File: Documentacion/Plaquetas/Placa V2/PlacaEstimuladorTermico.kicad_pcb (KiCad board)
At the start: 2 copper layers, 119.6 x 119.6 mm, 63 parts, among them J2 BorneraGrupoTermistores, J3 BorneraTermistor, J4 BORNERA_VCC, K1 FINDER-34.51, Q1 IRF4905, Q2 IRFZ44N, Q3 IRF4905, Q4 IRFZ44N, Q5 BC337, Q6 BC337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

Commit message: I designed the pcb, it was my first try so please check every wire
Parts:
- removed D5: DIODE, Diode_THT:D_5W_P10.16mm_Horizontal
- removed D6: D_Zener, Diode_THT:D_DO-201AE_P12.70mm_Horizontal
- removed K1: FINDER-34.51, Relay_THT:Relay_SPDT_Finder_34.51_Vertical
- removed R16, R17: R, Resistor_THT:R_Axial_DIN0309_L9.0mm_D3.2mm_P15.24mm_Horizontal
- removed RV1: R_POT, Potentiometer_THT:Potentiometer_ACP_CA14-H2,5_Horizontal
- removed SW1: SW_DIP_x01, TerminalBlock:TerminalBlock_bornier-2_P5.08mm
- added C11: 4.7n, Capacitor_THT:C_Disc_D7.0mm_W2.5mm_P5.00mm, B.Cu at (88.9, 86.9)
- A1, Q6, R11, U1, U4, U5: moved to B.Cu
- C1, C2: footprint Capacitor_THT:CP_Radial_D12.5mm_P5.00mm -> Capacitor_THT:CP_Radial_D13.0mm_P7.50mm
- C10, C6: footprint Capacitor_THT:C_Disc_D9.0mm_W5.0mm_P10.00mm -> Capacitor_THT:C_Disc_D7.0mm_W2.5mm_P5.00mm
- C3, C4: footprint Capacitor_THT:C_Disc_D9.0mm_W5.0mm_P10.00mm -> Capacitor_THT:C_Disc_D7.0mm_W2.5mm_P5.00mm; moved to B.Cu
- C5, C9: footprint Capacitor_THT:C_Radial_D8.0mm_H7.0mm_P3.50mm -> Capacitor_THT:C_Disc_D7.0mm_W2.5mm_P5.00mm
- R1, R13, R2: footprint Resistor_THT:R_Axial_DIN0309_L9.0mm_D3.2mm_P15.24mm_Horizontal -> Resistor_THT:R_Axial_DIN0204_L3.6mm_D1.6mm_P5.08mm_Horizontal; moved to B.Cu
- moved R12 338.8 mm to (163.7, 89.8), turned to 180 degrees
- moved R7 246.2 mm to (89.4, 80.8), turned to 180 degrees
- moved U5 229.8 mm to (74.7, 79.2), turned to 270 degrees
- moved R2 226.5 mm to (122.7, 102.1), turned to 270 degrees
- moved R11 223.4 mm to (95.6, 39.8)
- moved C4 209.2 mm to (128.3, 102.1), turned to 270 degrees
- moved R3 207.3 mm to (101.1, 77.7)
- moved C3 202.0 mm to (117.9, 116.8), turned to 270 degrees
- moved R4 198.2 mm to (82.2, 72.1)
- moved R15 196.4 mm to (127.3, 86.2)
- moved R5 195.4 mm to (87.4, 73.2)
- moved R1 195.0 mm to (113.3, 116.8), turned to 270 degrees
- moved R6 189.1 mm to (98.0, 90.4), turned to 90 degrees
- moved Q6 168.6 mm to (139.2, 81.0), turned to 180 degrees
- moved C6 167.8 mm to (99.6, 62.2), turned to 180 degrees
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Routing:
- net GND: track 33.2 -> 627.3 mm, vias 0 -> 7
- net VCC: track 38.2 -> 467.2 mm, vias 0 -> 4
- net PWM_FRIO: track 0.00 -> 171.4 mm
- net PMOS_CALOR: track 0.00 -> 170.0 mm
- net PIN-READY-LED-GREEN: track 0.00 -> 169.8 mm
- net PWM_CALOR: track 0.00 -> 164.1 mm
- net PIN-CAUTION-LED-YELLOW: track 0.00 -> 145.1 mm, vias 0 -> 2
- net Net-(D1-Pad2): track 0.00 -> 131.7 mm
- net PIN-WARNING-LED-RED: track 0.00 -> 120.2 mm, vias 0 -> 2
- net Net-(C10-Pad1): track 0.00 -> 108.5 mm
- net Net-(Q1-Pad1): track 0.00 -> 69.5 mm
- net PIN_SENSOR_TEMPERATURA_PUNTUAL: track 0.00 -> 65.4 mm
- net REF_OPAMPS: track 0.00 -> 63.7 mm
- net Net-(J3-Pad1): track 0.00 -> 62.2 mm
- net PMOS_FRIO: track 0.00 -> 58.6 mm
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- added copper zone on B.Cu, net GND
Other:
- board size 119.6 x 119.6 mm -> 147.8 x 128 mm

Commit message: Add files via upload
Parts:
- added D5: DIODE, Diode_THT:D_5W_P10.16mm_Horizontal, F.Cu at (144.0, 92.7)
- added D6: D_Zener, Diode_THT:D_DO-201AE_P12.70mm_Horizontal, F.Cu at (150.7, 90.3)
- added J1: Conn_01x02, custom_footprints:PinSocket_1x02_P2.54mm_Vertical, F.Cu at (255.1, 75.5)
- added J5: Conn_01x02, custom_footprints:disipadorFETS, F.Cu at (213.5, 103.0)
- added K1: Modulo_Relé, custom_footprints:Modulo_Relé_Arduino, F.Cu at (115.9, 92.3)
- added R16: R, Resistor_SMD:R_1206_3216Metric, B.Cu at (150.5, 79.3)
- added R17: R, Resistor_SMD:R_1206_3216Metric, B.Cu at (158.6, 94.2)
- added RV1: R_POT, Potentiometer_THT:Potentiometer_Bourns_3266Y_Vertical, F.Cu at (159.9, 85.5)
- added SW1: SW_DIP_x01, TerminalBlock:TerminalBlock_bornier-2_P5.08mm, F.Cu at (149.1, 128.5)
- A1: moved to F.Cu
- C10, C5, C6, C9: footprint Capacitor_THT:C_Disc_D7.0mm_W2.5mm_P5.00mm -> Capacitor_SMD:C_1206_3216Metric_Pad1.42x1.75mm_HandSolder; moved to B.Cu
- C11, C3, C4: footprint Capacitor_THT:C_Disc_D7.0mm_W2.5mm_P5.00mm -> Capacitor_SMD:C_1206_3216Metric_Pad1.42x1.75mm_HandSolder
- C8: footprint Capacitor_THT:C_Disc_D12.0mm_W4.4mm_P7.75mm -> Capacitor_SMD:C_1206_3216Metric_Pad1.42x1.75mm_HandSolder
- J2: value BorneraGrupoTermistores -> DB9_Female_MountingHoles; footprint TerminalBlock:TerminalBlock_bornier-2_P5.08mm -> Connector_Dsub:DSUB-9_Female_Horizontal_P2.77x2.84mm_EdgePinOffset7.70mm_Housed_MountingHolesOffset9.12mm
- J3: value BorneraTermistor -> Conn_01x01; footprint TerminalBlock:TerminalBlock_bornier-2_P5.08mm -> Connector:Banana_Jack_1Pin
- J4: value BORNERA_VCC -> Conn_01x01; footprint TerminalBlock:TerminalBlock_bornier-2_P5.08mm -> Connector:Banana_Jack_1Pin
- Q1, Q2, Q3, Q4: footprint Package_TO_SOT_THT:TO-220-3_Vertical -> custom_footprints:TO-220-3_Vertical
- Q5, Q7, Q8, Q9: footprint Package_TO_SOT_THT:TO-92_Inline -> custom_footprints:TO-92_HandSolder
- Q6, U5: footprint Package_TO_SOT_THT:TO-92_Inline -> custom_footprints:TO-92_HandSolder; moved to F.Cu
- R1, R13, R2: footprint Resistor_THT:R_Axial_DIN0204_L3.6mm_D1.6mm_P5.08mm_Horizontal -> Resistor_SMD:R_1206_3216Metric
- R10, R18, R19, R20, R3, R4, R5, R6, R7, R8, R9, U2, U3: moved to B.Cu
- R11: footprint Resistor_THT:R_Axial_DIN0309_L9.0mm_D3.2mm_P15.24mm_Horizontal -> Resistor_SMD:R_1206_3216Metric
- R12: footprint Resistor_THT:R_Axial_DIN0309_L9.0mm_D3.2mm_P15.24mm_Horizontal -> Resistor_SMD:R_1206_3216Metric; moved to B.Cu
- R14, R15: footprint Resistor_SMD:R_0805_2012Metric -> Resistor_SMD:R_1206_3216Metric; moved to B.Cu
- U1: footprint Package_DIP:DIP-14_W7.62mm_LongPads -> Package_DIP:DIP-14_W8.89mm_SMDSocket_LongPads
- U4: footprint Package_TO_SOT_THT:TO-220-3_Vertical -> custom_footprints:TO-220-3_Vertical; moved to F.Cu
- moved D7 210.8 mm to (254.8, 41.4), turned to 270 degrees
- moved Q7 202.8 mm to (238.9, 47.1)
- moved R18 190.4 mm to (245.4, 41.0), turned to 0 degrees
- moved D8 189.1 mm to (254.8, 51.7), turned to 270 degrees
- moved Q9 173.0 mm to (238.9, 53.5), turned to 90 degrees
- moved R20 172.2 mm to (245.4, 51.0)
- moved D9 167.0 mm to (254.8, 62.3), turned to 270 degrees
- moved J4 158.8 mm to (235.2, 73.3)
- moved Q8 155.7 mm to (238.9, 60.0), turned to 90 degrees
- moved C1 153.5 mm to (248.7, 152.7), turned to 0 degrees
- moved R19 153.3 mm to (245.4, 57.5)
- moved PELTIER1 151.1 mm to (219.6, 154.6), turned to 90 degrees
- moved C2 148.2 mm to (248.7, 135.0), turned to 0 degrees
- moved C9 133.0 mm to (200.2, 46.9), turned to 180 degrees
- moved D2 128.1 mm to (224.0, 135.9), turned to 0 degrees
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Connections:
- net Net-(C10-Pad1) renamed term_pelt_2
- A1 pad 10: PMOS_CALOR -> PWM_CALOR
- A1 pad 11: PMOS_FRIO -> PWM_FRIO
- A1 pad 15: PIN-READY-LED-GREEN -> Net-(A1-Pad15)
- A1 pad 20: PIN_SENSOR_TEMPERATURA_SUPERFICIAL -> PIN_SENSOR_TEMPERATURA_PUNTUAL
- A1 pad 21: PIN_SENSOR_TEMPERATURA_PUNTUAL -> PIN_SENSOR_TEMPERATURA_SUPERFICIAL
- A1 pad 7: Net-(A1-Pad7) -> PIN-READY-LED-GREEN
- A1 pad 8: PWM_CALOR -> PMOS_FRIO
- A1 pad 9: PWM_FRIO -> PMOS_CALOR
- C11 pad 1: Net-(C11-Pad1) -> term_disip_2
- J3 pad 1: Net-(J3-Pad1) -> VCC
- J4 pad 1: VCC -> GND
- R8 pad 1: Net-(C11-Pad1) -> term_disip_2
- U1 pad 12: Net-(C11-Pad1) -> term_disip_2
- U1 pad 8: Net-(J3-Pad1) -> term_disip_1
- U1 pad 9: Net-(J3-Pad1) -> term_disip_1
- U2 pad 3: Net-(U2-Pad3) -> PWM_FRIO
- U3 pad 3: Net-(U3-Pad3) -> PWM_CALOR
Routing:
- net GND: track 627.3 -> 978.6 mm, vias 7 -> 4
- net VCC: track 467.2 -> 701.3 mm, vias 4 -> 3
- net PMOS_CALOR: track 170.0 -> 24.3 mm
- net PIN-READY-LED-GREEN: track 169.8 -> 42.0 mm
- net PWM_CALOR: track 164.1 -> 40.0 mm
- net PWM_FRIO: track 171.4 -> 52.9 mm
- net PIN-CAUTION-LED-YELLOW: track 145.1 -> 45.2 mm, vias 2 -> 0
- net PIN-WARNING-LED-RED: track 120.2 -> 50.8 mm, vias 2 -> 0
- net Net-(D5-Pad2): track 0.00 -> 64.0 mm
- net Net-(D6-Pad1): track 0.00 -> 63.7 mm, vias 0 -> 1
- net Net-(J3-Pad1): track 62.2 -> 0.00 mm
- net Net-(RV1-Pad2): track 0.00 -> 59.5 mm, vias 0 -> 2
- net Net-(D5-Pad1): track 0.00 -> 55.6 mm, vias 0 -> 1
- net Net-(D1-Pad2): track 131.7 -> 79.2 mm
- net Net-(C11-Pad1): track 46.1 -> 0.00 mm
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- removed copper zone on B.Cu, net GND
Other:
- board size 147.8 x 128 mm -> 152.4 x 149.9 mm
- net class Default: clearance 0.2 -> 0.3; trace_width 0.25 -> 1; via_dia 0.8 -> 2; via_drill 0.4 -> 1
- net class Power added: clearance 0.5, trace_width 3, via_dia 2, via_drill 1
- rule trace_clearance: 0.2 -> 0.3
- rule via_min_size: 0.4 -> 0.1
- board text added: "DB9 PELTIER"
- board text added: "POWER"
- board text added: "USB LEDS PULSADOR"

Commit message: Correction of all the errors in the pcb
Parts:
- removed D6: D_Zener, Diode_THT:D_DO-201AE_P12.70mm_Horizontal
- removed R16: R, Resistor_SMD:R_1206_3216Metric
- added J6: Pulsador OFF, TerminalBlock:TerminalBlock_bornier-2_P5.08mm, F.Cu at (151.7, 126.3)
- added J7: Conn_02x04_Counter_Clockwise, Package_DIP:DoublePin, F.Cu at (120.6, 43.0)
- added J8: Conn_02x04_Counter_Clockwise, Package_DIP:DoublePin, F.Cu at (77.5, 35.8)
- added R21: 15, Resistor_THT:R_Axial_DIN0204_L3.6mm_D1.6mm_P5.08mm_Horizontal, B.Cu at (226.2, 112.9)
- added R22: 15, Resistor_THT:R_Axial_DIN0204_L3.6mm_D1.6mm_P5.08mm_Horizontal, B.Cu at (209.2, 110.4)
- added U6: TL431LP, Package_TO_SOT_THT:TO-92_Inline, F.Cu at (153.9, 103.9)
- SW1: value SW_DIP_x01 -> Pulsador ON
- moved J2 55.4 mm to (64.8, 45.0)
- moved SW1 17.2 mm to (166.1, 130.7)
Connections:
- A1 pad 29: GND -> fan_2
- A1 pad 4: GND -> fan_2
- C1 pad 2: GND -> fan_2
- C10 pad 2: GND -> fan_2
- C11 pad 2: GND -> fan_2
- C2 pad 2: GND -> fan_2
- C3 pad 2: GND -> fan_2
- C4 pad 2: GND -> fan_2
- C5 pad 2: GND -> fan_2
- C6 pad 2: GND -> fan_2
- C7 pad 2: GND -> fan_2
- C8 pad 2: GND -> fan_2
- C9 pad 2: GND -> fan_2
- D2 pad 2: GND -> fan_2
- D4 pad 2: GND -> fan_2
- J1 pad 2: GND -> fan_2
- J2 pad 0: GND -> fan_2C
- J2 pad 1: REF_OPAMPS -> term_disip_2C
- J2 pad 2: term_pelt_2 -> term_disip_1C
- J2 pad 3: term_disip_1 -> term_pelt_2C
- J2 pad 4: term_disip_2 -> term_pelt_1C
- J2 pad 5: GND -> Net-(J2-Pad5)
- J2 pad 6: Net-(J2-Pad6) -> fan_1C
- J2 pad 9: VCC -> fan_2C
- J4 pad 1: GND -> fan_2
- K1 pad 1: Net-(D5-Pad2) -> inPowerSupply
- K1 pad 2: GND -> fan_2
- K1 pad 3: VCC -> Net-(J6-Pad1)
- Q2 pad 3: GND -> fan_2
- Q4 pad 3: GND -> fan_2
- Q5 pad 3: GND -> fan_2
- Q6 pad 3: GND -> fan_2
- R1 pad 2: GND -> fan_2
- R18 pad 2: GND -> fan_2
- R19 pad 2: GND -> fan_2
- R2 pad 2: GND -> fan_2
- R20 pad 2: GND -> fan_2
- R3 pad 2: GND -> fan_2
- R5 pad 2: GND -> fan_2
- R7 pad 2: GND -> fan_2
- R8 pad 2: GND -> fan_2
- R9 pad 2: GND -> fan_2
- RV1 pad 1: GND -> fan_2
- U1 pad 11: GND -> fan_2
- U2 pad 3: PWM_FRIO -> Net-(U2-Pad3)
- U2 pad 4: GND -> fan_2
- U2 pad 5: GND -> fan_2
- U2 pad 6: Net-(Q4-Pad1) -> Net-(R21-Pad2)
- U2 pad 7: Net-(Q4-Pad1) -> Net-(R21-Pad2)
- U3 pad 3: PWM_CALOR -> Net-(U3-Pad3)
- U3 pad 4: GND -> fan_2
- U3 pad 5: GND -> fan_2
- U3 pad 6: Net-(Q2-Pad1) -> Net-(R22-Pad2)
- U3 pad 7: Net-(Q2-Pad1) -> Net-(R22-Pad2)
- U4 pad 2: GND -> fan_2
- U5 pad 2: GND -> fan_2
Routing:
- net fan_2: track 0.00 -> 1032.2 mm, vias 0 -> 6
- net GND: track 978.6 -> 0.00 mm, vias 4 -> 0
- net VCC: track 701.3 -> 792.0 mm, vias 3 -> 4
- net fan_2C: track 0.00 -> 81.6 mm
- net Net-(D6-Pad2): track 26.1 -> 0.00 mm
- net fan_1C: track 0.00 -> 25.4 mm
- net Net-(R17-Pad2): track 63.7 -> 80.2 mm, vias 1 -> 2
- net inPowerSupply: track 37.3 -> 53.1 mm
- net term_disip_2C: track 0.00 -> 13.3 mm
- net term_disip_1C: track 0.00 -> 13.2 mm
- net term_pelt_2C: track 0.00 -> 13.1 mm
- net term_pelt_1C: track 0.00 -> 13.0 mm
- net Net-(Q2-Pad1): track 15.4 -> 4.82 mm
- net Net-(R21-Pad2): track 0.00 -> 8.21 mm
- net Net-(D5-Pad2): track 64.0 -> 57.7 mm, vias 0 -> 1
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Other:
- board size 152.4 x 149.9 mm -> 207.5 x 149.9 mm

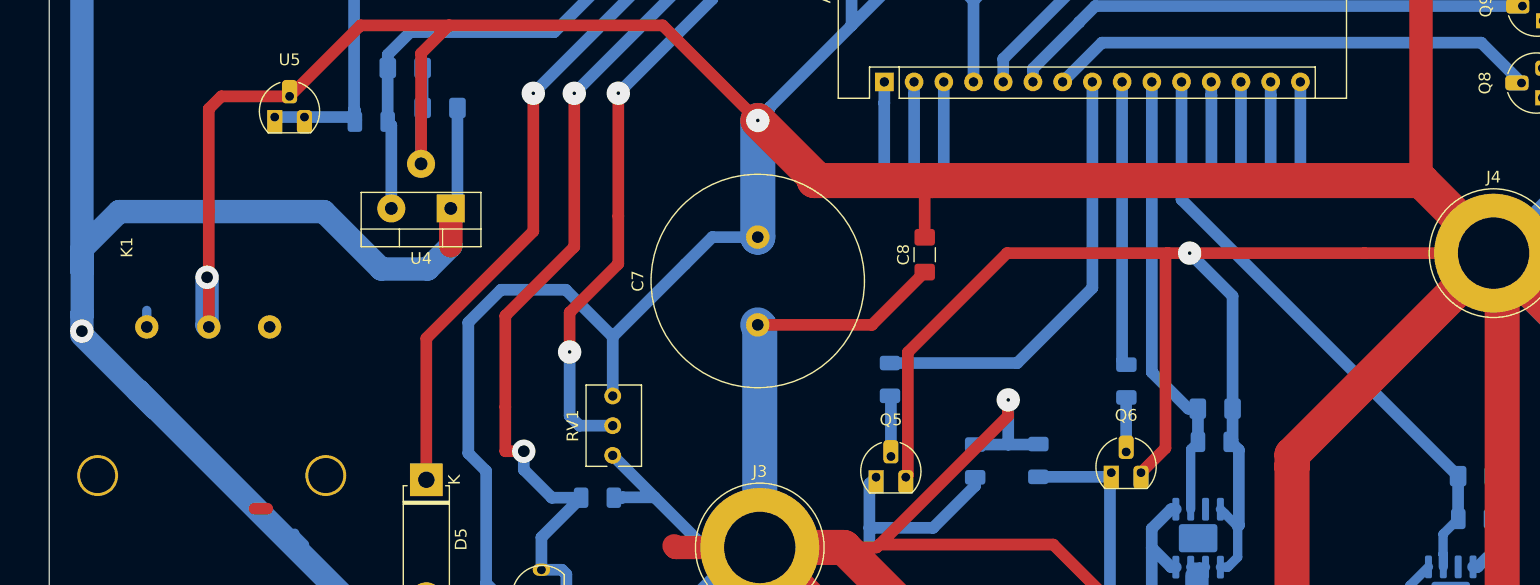
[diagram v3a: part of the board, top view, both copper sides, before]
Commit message: Correction of pwm pins
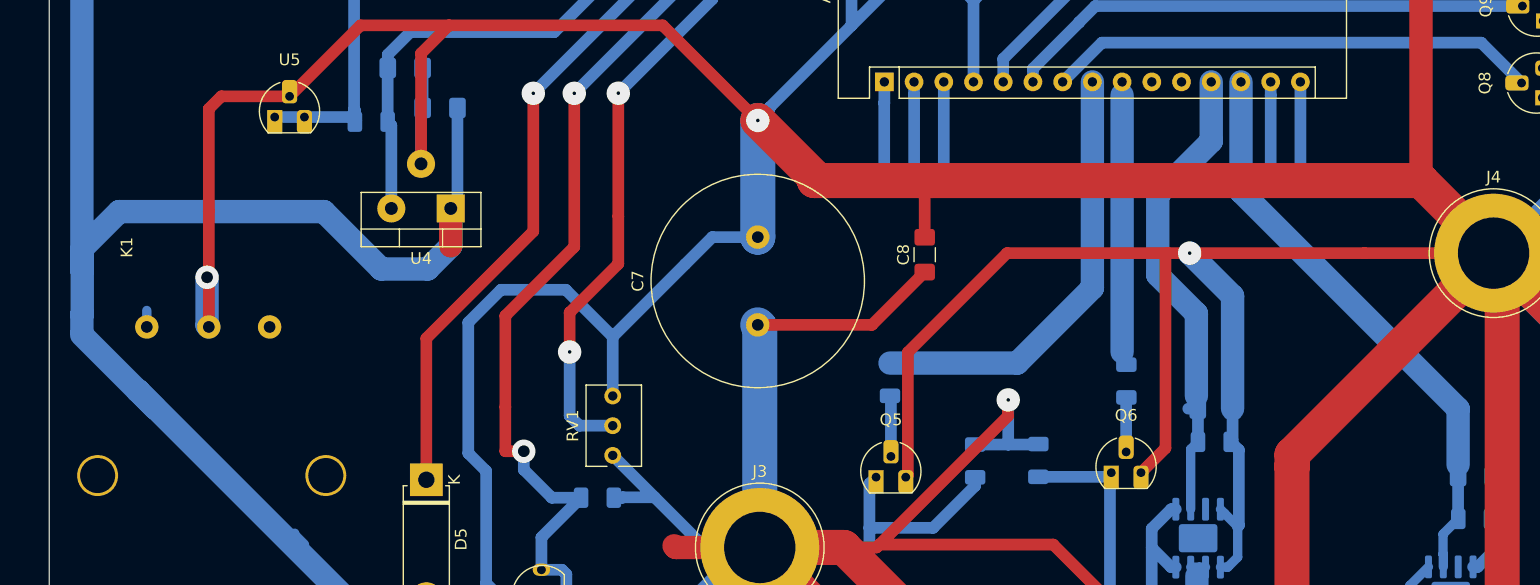
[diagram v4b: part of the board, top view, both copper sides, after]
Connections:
- A1 pad 10: PWM_CALOR -> Net-(A1-Pad10)
- A1 pad 11: PWM_FRIO -> Net-(A1-Pad11)
- A1 pad 12: Net-(A1-Pad12) -> PWM_CALOR
- A1 pad 13: Net-(A1-Pad13) -> PWM_FRIO
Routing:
- net Net-(A1-Pad12): track 8.89 -> 0.00 mm
- net Net-(A1-Pad13): track 8.67 -> 0.00 mm
- net PWM_CALOR: track 39.0 -> 42.2 mm
- net PWM_FRIO: track 51.8 -> 49.7 mm
- net VCC: track 792.0 -> 790.5 mm, vias 4 -> 3
- net PMOS_CALOR: track 24.3 -> 24.8 mm
